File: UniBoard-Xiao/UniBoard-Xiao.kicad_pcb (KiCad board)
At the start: 2 copper layers, 100 x 100 mm, 40 parts, among them J1 tirette, J10 I2C Extension, J11 LIDAR, J12 5vp, J13 5vp, J14 5vp, J15 ultrasonic sensor, J3 BAU, J4 oled I2C, J5 STEPPER D, J6 STEPPER G, J7 I2C Extension, J8 con BAT, J9 I2C Extension, SW1 SW_DIP_x02, SW2 SW_DIP_x02, U1 XIAO-ESP32-S3-DIP, U2 TMC2209_SILENTSTEPSTICK, U3 TMC2209_SILENTSTEPSTICK, U4 TSR1-2433E, U5 TSR2-2450N, U6 TSR1-2450E

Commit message: New-placement
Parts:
- moved J14 93.5 mm to (195.2, 111.9), turned to 180 degrees
- moved J12 91.7 mm to (195.1, 129.9), turned to 180 degrees
- moved J13 90.9 mm to (195.2, 120.9), turned to 180 degrees
- moved J8 87.1 mm to (185.7, 140.4), turned to 180 degrees
- moved PS1 82.8 mm to (178.9, 59.1), turned to -90 degrees
- moved J6 80.8 mm to (111.9, 139.9), turned to 0 degrees
- moved J3 75.8 mm to (167.2, 140.4)
- moved C1 64.4 mm to (127.5, 136.9), turned to -90 degrees
- moved J10 64.4 mm to (134.9, 93.5)
- moved J4 64.4 mm to (134.9, 69.5)
- moved J7 64.4 mm to (134.9, 77.5)
- moved J9 64.4 mm to (134.9, 85.5)
- moved J15 63.8 mm to (156.1, 73.6), turned to 180 degrees
- moved J5 63.3 mm to (136.5, 139.9), turned to 0 degrees
- moved D5 63.2 mm to (178.0, 121.0), turned to 90 degrees
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
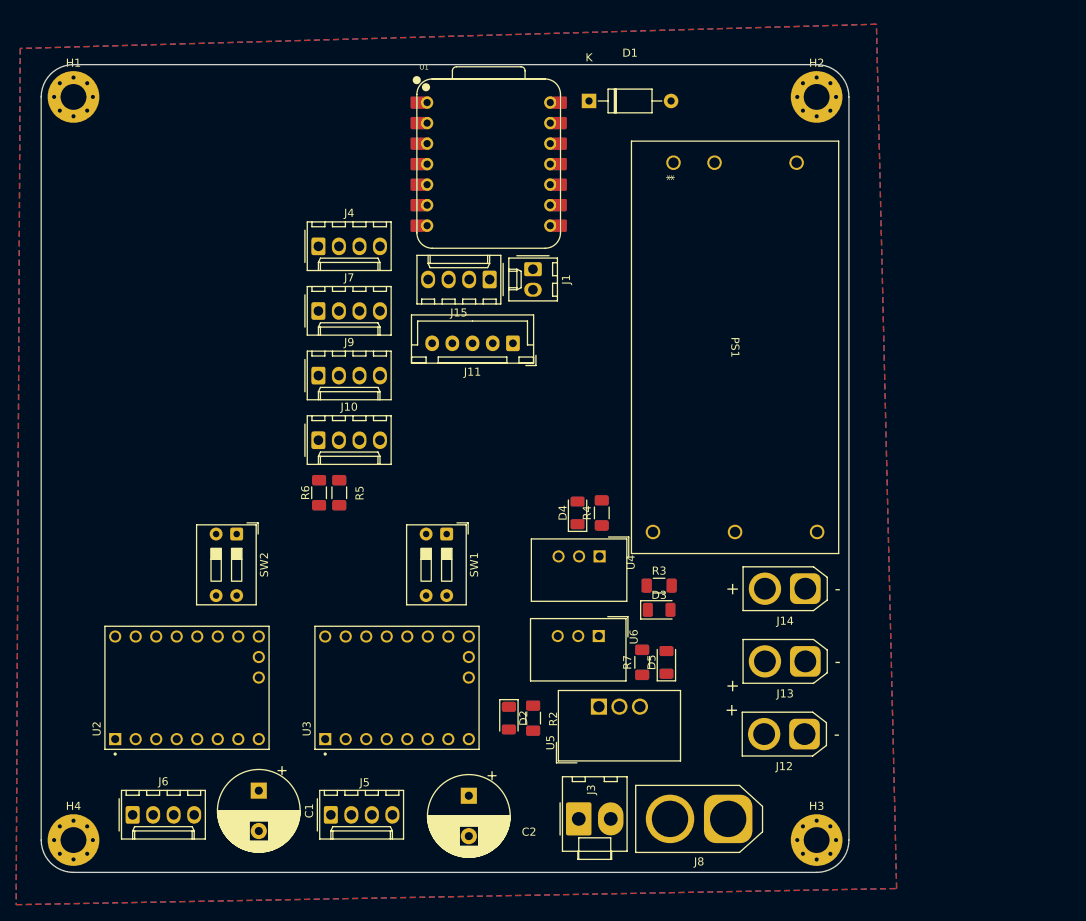
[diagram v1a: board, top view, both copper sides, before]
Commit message: Rescale to 8*8
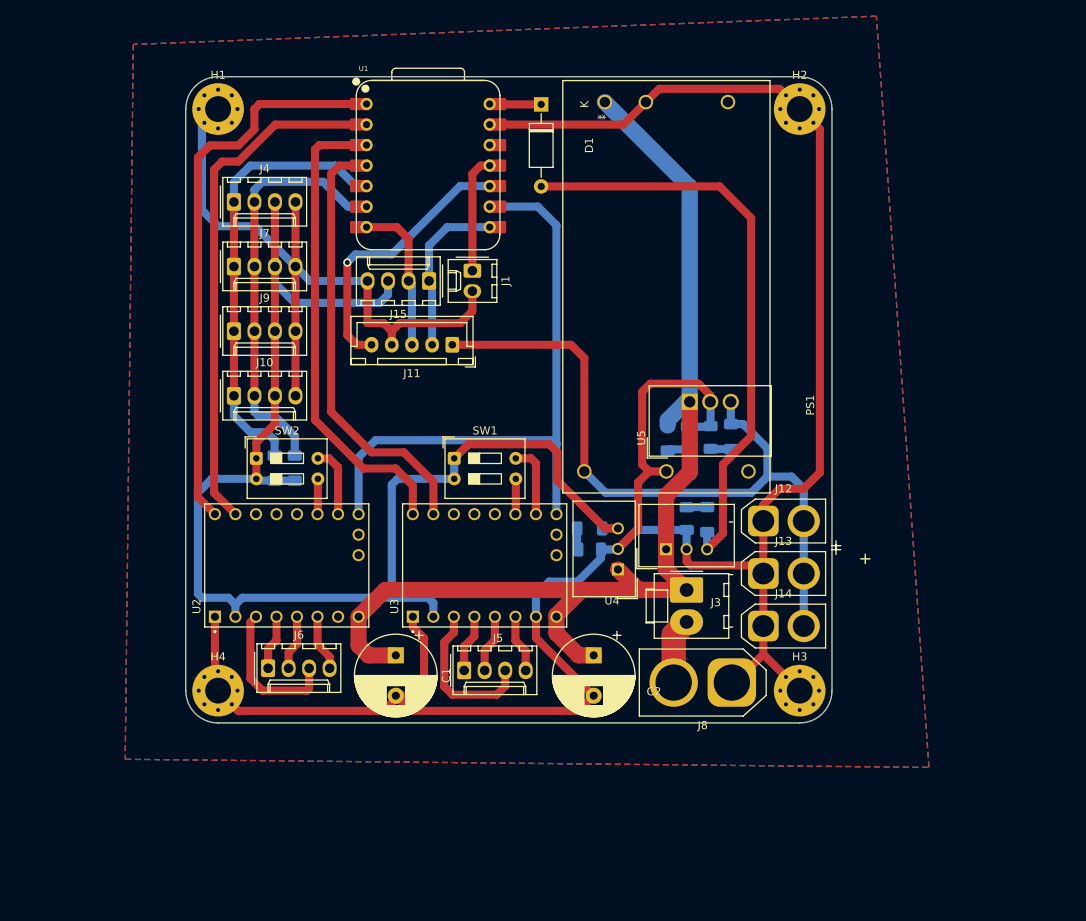
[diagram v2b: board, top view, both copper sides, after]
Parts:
- D2, D3, D4, D5, R2, R3, R4, R5, R6, R7: moved to B.Cu
- moved U5 39.4 mm to (180.9, 88.8)
- moved D2 33.1 mm to (180.5, 103.2), turned to 90 degrees
- moved R2 32.7 mm to (183.1, 103.3), turned to 90 degrees
- moved J3 31.3 mm to (180.5, 112.0), turned to -90 degrees
- moved R7 30.0 mm to (186.0, 93.0), turned to -90 degrees
- moved D5 28.4 mm to (183.5, 93.2), turned to -90 degrees
- moved J12 26.9 mm to (190.0, 103.5), turned to 0 degrees
- moved H4 25.7 mm to (122.5, 124.5)
- moved J6 24.7 mm to (128.7, 121.7)
- moved J5 24.3 mm to (153.0, 122.0)
- moved C1 23.8 mm to (144.5, 120.1)
- moved C2 23.3 mm to (169.0, 120.1)
- moved U2 19.5 mm to (131.0, 109.0)
- moved U3 18.6 mm to (155.5, 109.0)
- moved H3 18.6 mm to (194.5, 124.5)
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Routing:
- net GND: track 0.00 -> 375.5 mm
- net +3.3V: track 0.00 -> 167.1 mm
- net +24V: track 0.00 -> 139.4 mm
- net +5VP: track 0.00 -> 89.8 mm
- net EN: track 0.00 -> 77.6 mm
- net +5V: track 0.00 -> 73.0 mm
- net DIR G: track 0.00 -> 69.3 mm
- net STEP G: track 0.00 -> 64.1 mm
- net DIR D: track 0.00 -> 59.1 mm
- net SDA: track 0.00 -> 55.4 mm
- net STEP D: track 0.00 -> 53.7 mm
- net SCL: track 0.00 -> 51.7 mm
- net Lidar_PWM: track 0.00 -> 34.0 mm, vias 0 -> 1
- net TX-LIDAR: track 0.00 -> 21.0 mm
- net Net-(J5-Pin_3): track 0.00 -> 19.5 mm
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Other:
- board size 100 x 100 mm -> 80 x 80 mm

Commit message: adjustment
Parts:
- moved J10 0.52 mm to (124.5, 88.5)
- moved J6 0.23 mm to (128.7, 121.5)
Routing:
- net +24V: track 139.4 -> 138.5 mm
- net EN: track 77.6 -> 78.2 mm
- net Net-(J6-Pin_3): track 18.4 -> 17.9 mm

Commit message: End of routing
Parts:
- SW1, SW2: moved to B.Cu
- moved SW2 13.7 mm to (127.3, 109.5)
- moved SW1 13.7 mm to (151.6, 109.5)
- moved R5 5.38 mm to (124.5, 95.0)
- moved R6 5.38 mm to (127.0, 95.0)
- moved D4 4.13 mm to (180.6, 89.1)
- moved D5 4.13 mm to (183.4, 89.0)
- moved R4 4.13 mm to (178.1, 89.1)
- moved R7 4.13 mm to (185.9, 88.9)
- moved U5 4.13 mm to (180.8, 84.6)
- moved J1 3.84 mm to (156.5, 75.4), turned to 0 degrees
- moved J11 2.39 mm to (151.5, 84.1)
- moved J15 1.72 mm to (149.1, 75.4)
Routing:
- net GND: track 375.7 -> 0.00 mm
- net +24V: track 138.5 -> 146.8 mm
- net Net-(J5-Pin_3): track 19.2 -> 12.0 mm
- net Net-(J6-Pin_3): track 17.9 -> 11.9 mm
- net SDA: track 55.4 -> 49.7 mm
- net SCL: track 51.7 -> 46.0 mm
- net DIR D: track 59.1 -> 54.3 mm
- net TIRETTE: track 14.6 -> 19.3 mm
- net DIR G: track 69.3 -> 65.0 mm
- net +5V: track 73.0 -> 69.0 mm
- net +5VP: track 89.8 -> 92.7 mm
- net RX-LIDAR: track 19.1 -> 21.5 mm
- net STEP D: track 53.7 -> 51.5 mm
- net TX-LIDAR: track 21.0 -> 23.0 mm
- net Lidar_PWM: track 34.0 -> 35.4 mm
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
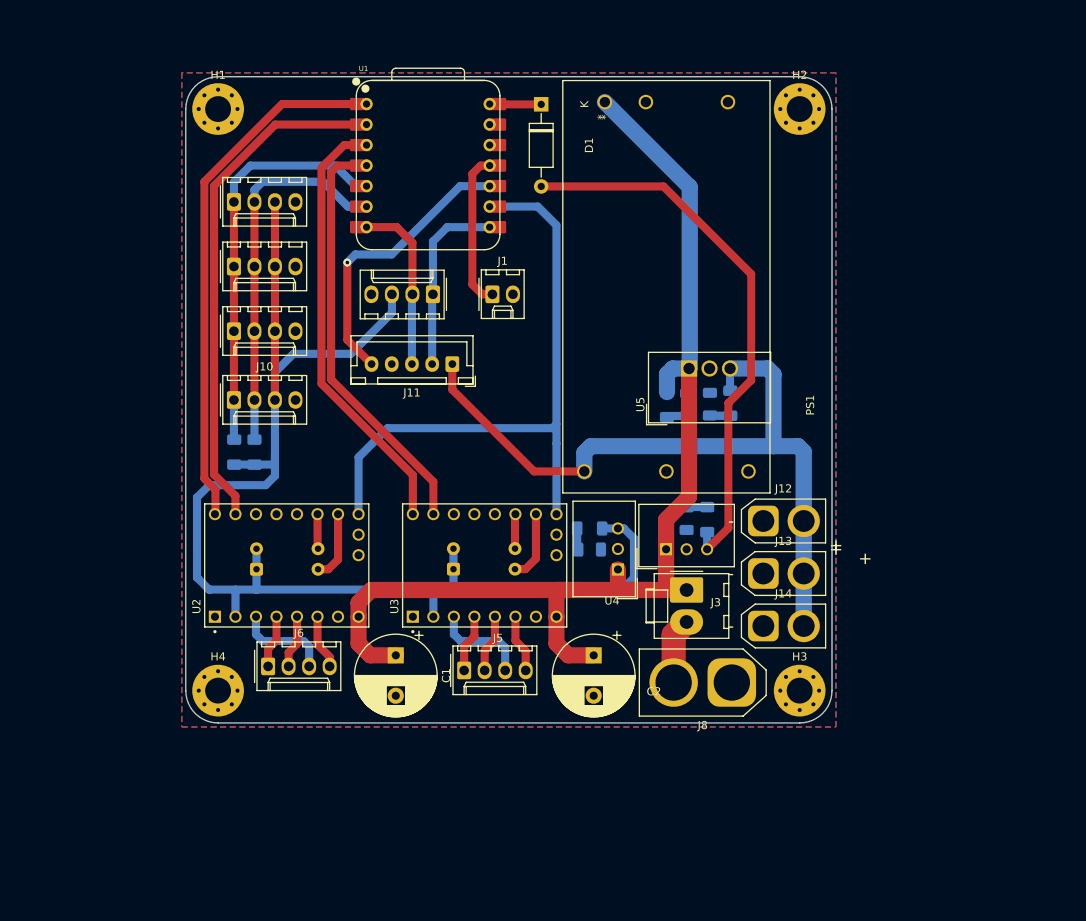
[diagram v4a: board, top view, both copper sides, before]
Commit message: begin silkscreen
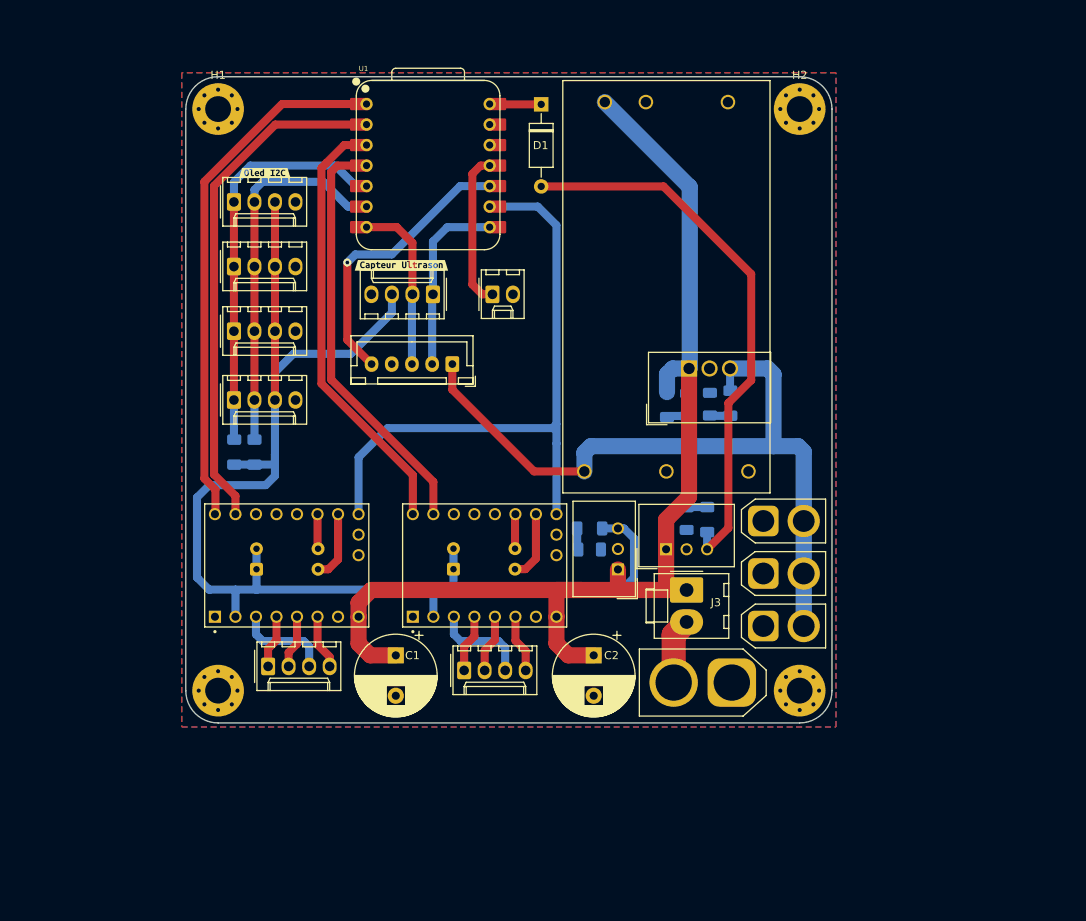
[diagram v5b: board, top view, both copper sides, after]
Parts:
- added kibuzzard-67ED5DC2: G***, kibuzzard-67ED5DC2, F.Cu at (128.3, 60.4)
- added kibuzzard-67ED5E40: G***, kibuzzard-67ED5E40, F.Cu at (145.2, 71.8)
- added kibuzzard-67ED5E55: G***, kibuzzard-67ED5E55, B.Cu at (141.5, 72.9)
- added kibuzzard-67ED5E7B: G***, kibuzzard-67ED5E7B, B.Cu at (144.0, 72.9)
- added kibuzzard-67ED5E8C: G***, kibuzzard-67ED5E8C, B.Cu at (149.1, 72.6)
- added kibuzzard-67ED5EA2: G***, kibuzzard-67ED5EA2, B.Cu at (146.6, 72.5)
- added kibuzzard-67ED5FB9: G***, kibuzzard-67ED5FB9, B.Cu at (124.5, 109.5)
- added kibuzzard-67ED5FB9: G***, kibuzzard-67ED5FB9, B.Cu at (148.5, 109.5)
- added kibuzzard-67ED5FC6: G***, kibuzzard-67ED5FC6, B.Cu at (124.5, 106.9)
- added kibuzzard-67ED5FC6: G***, kibuzzard-67ED5FC6, B.Cu at (148.5, 106.9)

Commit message: End Label
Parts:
- removed kibuzzard-67ED5E40: G***, kibuzzard-67ED5E40
- removed the kibuzzard-67ED5E55 at (141.5, 72.9)
- removed the kibuzzard-67ED5FB9 at (124.5, 109.5)
- added kibuzzard-67ED5E55: G***, kibuzzard-67ED5E55, B.Cu at (190.0, 99.8)
- added kibuzzard-67ED5E55: G***, kibuzzard-67ED5E55, B.Cu at (153.9, 54.4)
- added kibuzzard-67ED5E55: G***, kibuzzard-67ED5E55, B.Cu at (189.2, 126.7)
- added kibuzzard-67ED5E7B: G***, kibuzzard-67ED5E7B, B.Cu at (124.7, 113.1)
- added kibuzzard-67ED5E7B: G***, kibuzzard-67ED5E7B, B.Cu at (149.1, 113.1)
- added kibuzzard-67ED5E7B: G***, kibuzzard-67ED5E7B, B.Cu at (129.6, 69.6)
- added kibuzzard-67ED60FC: G***, kibuzzard-67ED60FC, F.Cu at (146.5, 87.2)
- added kibuzzard-67ED6169: G***, kibuzzard-67ED6169, F.Cu at (128.5, 68.5)
- added kibuzzard-67ED6169: G***, kibuzzard-67ED6169, F.Cu at (128.3, 76.5)
- added kibuzzard-67ED6169: G***, kibuzzard-67ED6169, F.Cu at (128.3, 85.0)
- added kibuzzard-67ED61B4: G***, kibuzzard-67ED61B4, F.Cu at (145.2, 71.8)
- added kibuzzard-67ED6224: G***, kibuzzard-67ED6224, F.Cu at (161.0, 75.4)
- added kibuzzard-67ED70B6: G***, kibuzzard-67ED70B6, F.Cu at (178.0, 49.7)
- added kibuzzard-67ED71A8: G***, kibuzzard-67ED71A8, F.Cu at (170.3, 112.3)
- added kibuzzard-67ED71B1: G***, kibuzzard-67ED71B1, F.Cu at (183.3, 90.8)
- added kibuzzard-67ED71DE: G***, kibuzzard-67ED71DE, F.Cu at (180.4, 102.0)
- added kibuzzard-67ED725F: G***, kibuzzard-67ED725F, F.Cu at (174.9, 113.8)
- added kibuzzard-67ED72B0: G***, kibuzzard-67ED72B0, F.Cu at (138.1, 100.8)
- added kibuzzard-67ED72B6: G***, kibuzzard-67ED72B6, F.Cu at (162.6, 100.8)
- added kibuzzard-67ED72F3: G***, kibuzzard-67ED72F3, F.Cu at (156.8, 125.7)
- added kibuzzard-67ED72FD: G***, kibuzzard-67ED72FD, F.Cu at (132.5, 125.1)
- added kibuzzard-67ED73B3: G***, kibuzzard-67ED73B3, B.Cu at (155.4, 112.6)
- added kibuzzard-67ED73B3: G***, kibuzzard-67ED73B3, B.Cu at (131.1, 112.6)
- added kibuzzard-67ED7493: G***, kibuzzard-67ED7493, F.Cu at (148.5, 49.5)
- added kibuzzard-67ED7EA6: G***, kibuzzard-67ED7EA6, B.Cu at (127.0, 69.6)
- added kibuzzard-67ED7EC9: G***, kibuzzard-67ED7EC9, B.Cu at (124.5, 69.6)
- added kibuzzard-67ED8061: G***, kibuzzard-67ED8061, B.Cu at (169.0, 117.0)
- added kibuzzard-67ED8061: G***, kibuzzard-67ED8061, B.Cu at (164.4, 112.7)
- added kibuzzard-67ED8061: G***, kibuzzard-67ED8061, B.Cu at (167.6, 51.7)
- added kibuzzard-67ED8061: G***, kibuzzard-67ED8061, B.Cu at (139.9, 112.7)
- added kibuzzard-67ED8061: G***, kibuzzard-67ED8061, B.Cu at (169.2, 109.5)
- added kibuzzard-67ED8061: G***, kibuzzard-67ED8061, B.Cu at (178.0, 104.1)
- added kibuzzard-67ED80BA: G***, kibuzzard-67ED80BA, B.Cu at (151.5, 81.5)
- added kibuzzard-67ED80BA: G***, kibuzzard-67ED80BA, B.Cu at (194.9, 99.4)
- added kibuzzard-67ED8412: G***, kibuzzard-67ED8412, B.Cu at (154.2, 67.2)
- added kibuzzard-67ED8447: G***, kibuzzard-67ED8447, B.Cu at (154.2, 64.7)
- added kibuzzard-67ED8456: G***, kibuzzard-67ED8456, B.Cu at (153.9, 62.1)
- added kibuzzard-67ED8466: G***, kibuzzard-67ED8466, B.Cu at (152.6, 59.5)
- added kibuzzard-67ED8504: G***, kibuzzard-67ED8504, B.Cu at (142.8, 67.1)
- added kibuzzard-67ED8648: G***, kibuzzard-67ED8648, B.Cu at (153.9, 51.9)
- added kibuzzard-67ED86A2: G***, kibuzzard-67ED86A2, B.Cu at (143.8, 56.9)
- added kibuzzard-67ED86A7: G***, kibuzzard-67ED86A7, B.Cu at (144.1, 59.5)
- added kibuzzard-67ED86B0: G***, kibuzzard-67ED86B0, B.Cu at (144.1, 54.4)
- added kibuzzard-67ED86BE: G***, kibuzzard-67ED86BE, B.Cu at (143.8, 51.9)
- added kibuzzard-67ED86D2: G***, kibuzzard-67ED86D2, B.Cu at (143.1, 64.6)
- added kibuzzard-67ED86DD: G***, kibuzzard-67ED86DD, B.Cu at (143.2, 62.0)
- added kibuzzard-67ED8D70: G***, kibuzzard-67ED8D70, B.Cu at (124.0, 109.4)
- added kibuzzard-67ED8D8D: G***, kibuzzard-67ED8D8D, B.Cu at (146.6, 100.4)
- added kibuzzard-67ED8D8D: G***, kibuzzard-67ED8D8D, B.Cu at (122.1, 100.4)
- added kibuzzard-67ED8DB2: G***, kibuzzard-67ED8DB2, B.Cu at (124.7, 100.0)
- added kibuzzard-67ED8DB2: G***, kibuzzard-67ED8DB2, B.Cu at (149.2, 100.0)
- added kibuzzard-67ED8DD6: G***, kibuzzard-67ED8DD6, B.Cu at (164.4, 100.7)
- added kibuzzard-67ED8DD6: G***, kibuzzard-67ED8DD6, B.Cu at (139.9, 100.7)
- added kibuzzard-67ED90FC: G***, kibuzzard-67ED90FC, B.Cu at (187.6, 89.1)
- added kibuzzard-67ED90FC: G***, kibuzzard-67ED90FC, B.Cu at (184.7, 103.3)
- added kibuzzard-67ED90FC: G***, kibuzzard-67ED90FC, B.Cu at (128.6, 95.0)
- added kibuzzard-67ED911B: G***, kibuzzard-67ED911B, B.Cu at (122.9, 95.0)
- added kibuzzard-67ED911B: G***, kibuzzard-67ED911B, B.Cu at (176.4, 89.1)
- added kibuzzard-67ED911B: G***, kibuzzard-67ED911B, B.Cu at (168.5, 102.8)
- added kibuzzard-67ED922B: G***, kibuzzard-67ED922B, B.Cu at (184.7, 112.0)
- moved kibuzzard-67ED5FC6 0.44 mm to (124.0, 107.0)
- moved kibuzzard-67ED5EA2 0.15 mm to (146.6, 72.7)
- moved kibuzzard-67ED5E7B 0.13 mm to (144.0, 73.0)
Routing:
- net TIRETTE: track 19.3 -> 21.9 mm
- net EN: track 78.2 -> 76.1 mm
- net Lidar_PWM: vias 1 -> 0

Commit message: final fixes
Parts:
- removed kibuzzard-67ED73B3 (x2): G***, kibuzzard-67ED73B3
- added kibuzzard-67EE6BB1: G***, kibuzzard-67EE6BB1, B.Cu at (155.4, 112.6)
- added kibuzzard-67EE6BB9: G***, kibuzzard-67EE6BB9, B.Cu at (131.1, 112.6)
